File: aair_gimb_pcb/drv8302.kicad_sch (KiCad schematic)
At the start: 15 parts, among them U1 DRV8302

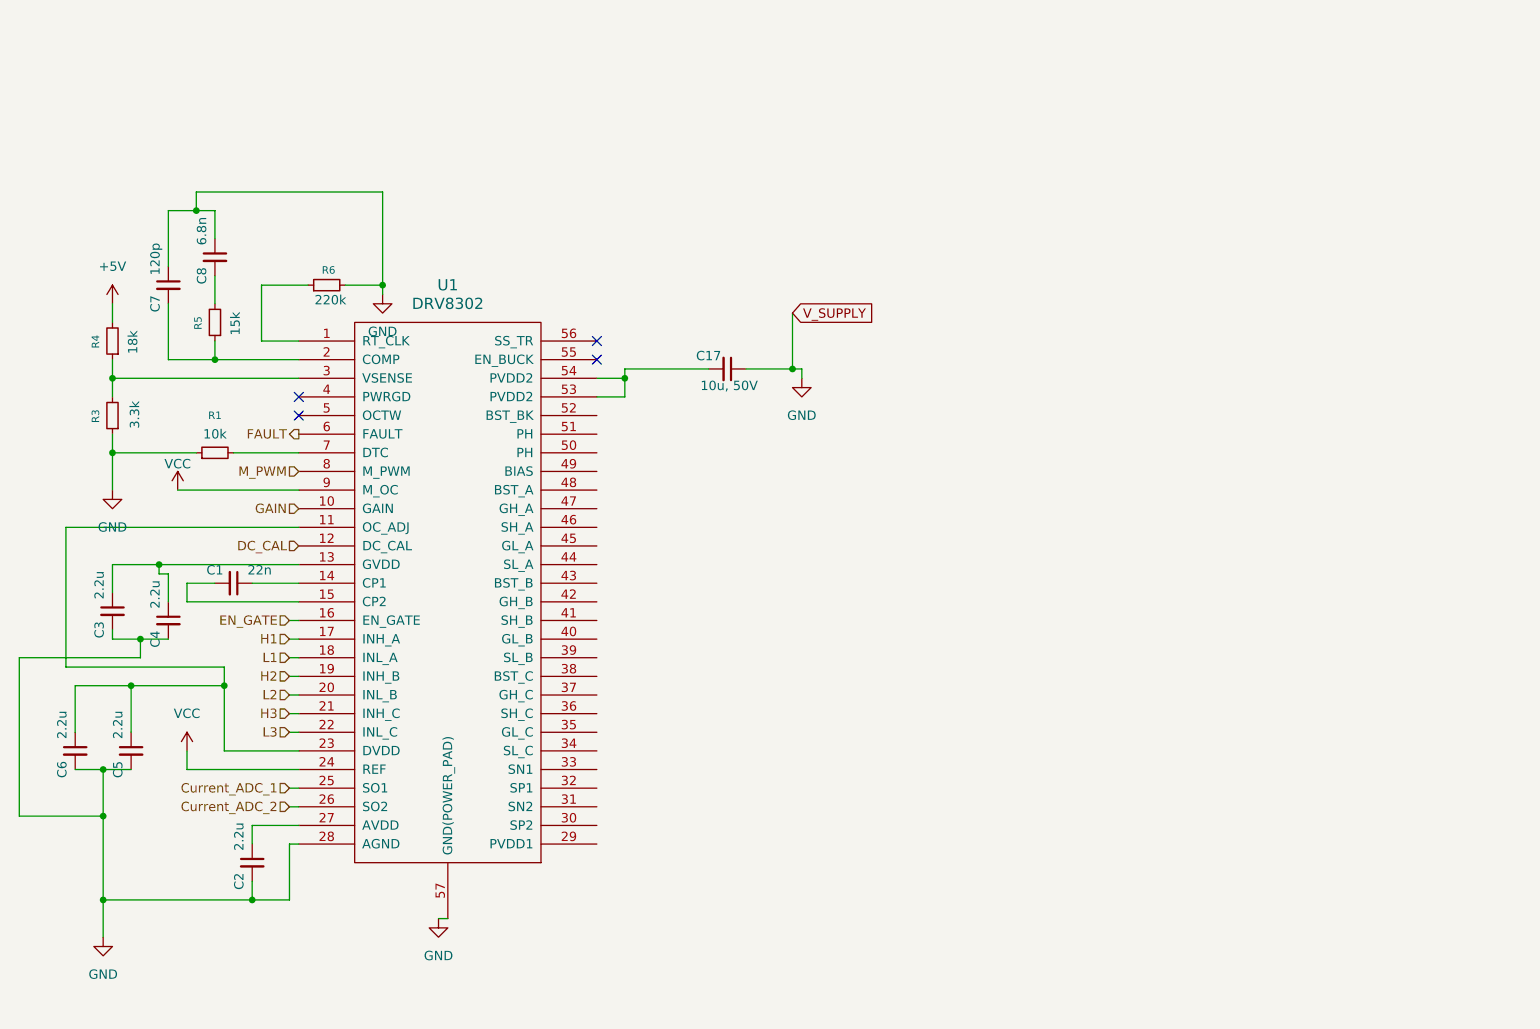
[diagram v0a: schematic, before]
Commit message: add mosfet
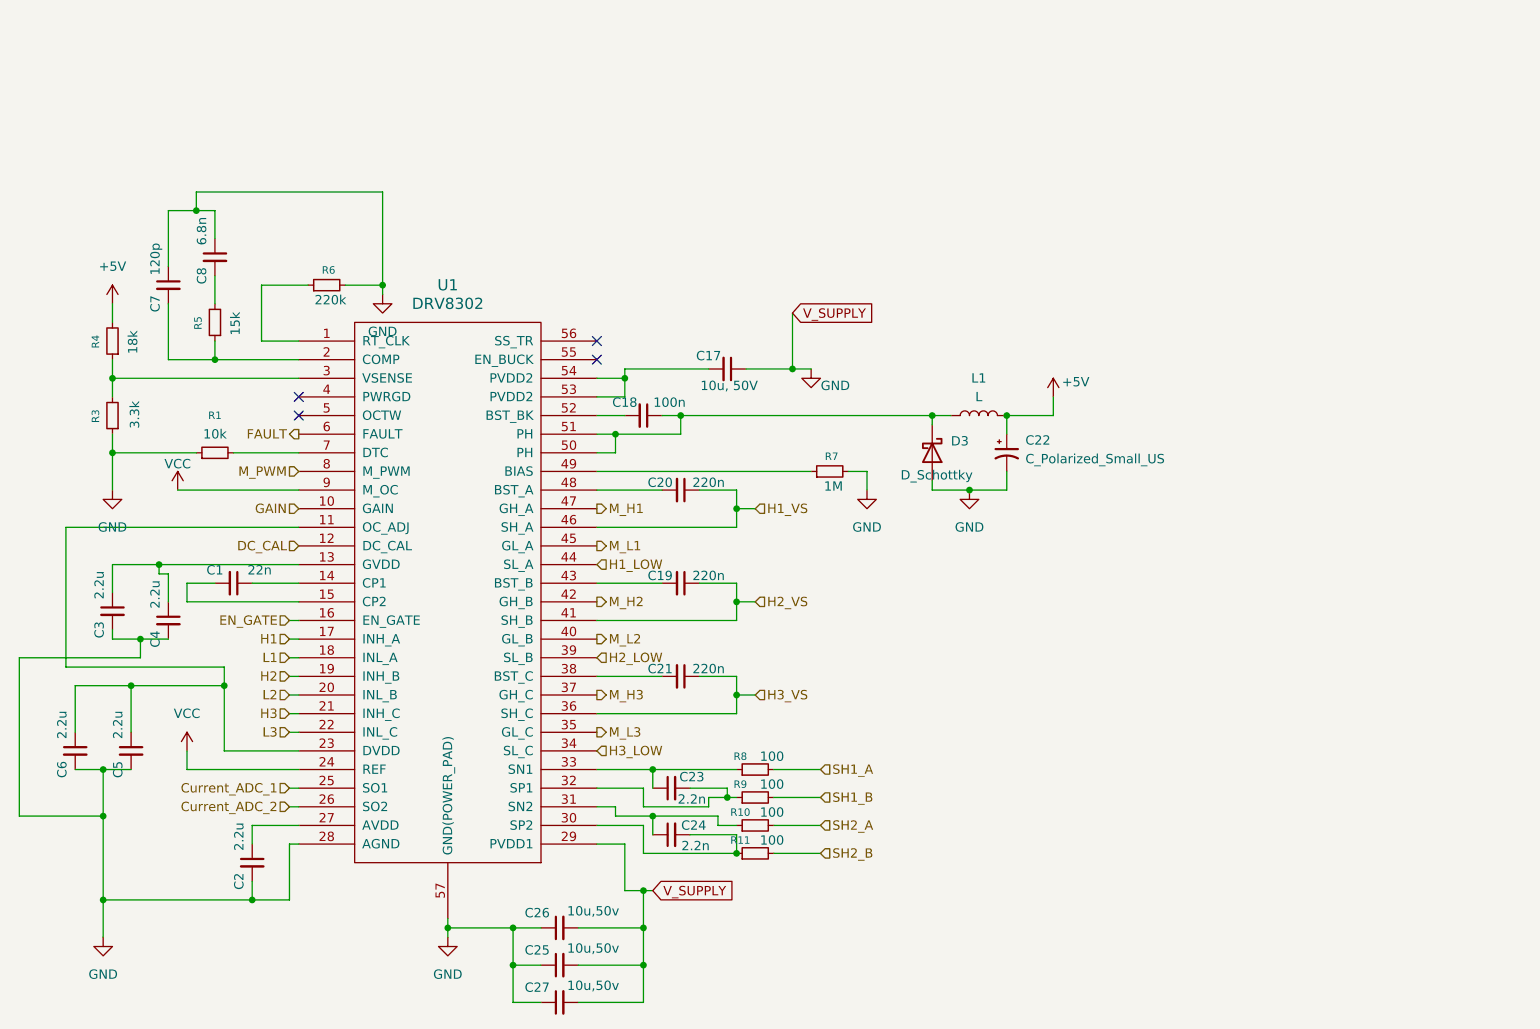
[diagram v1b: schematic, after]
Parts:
- added C18: 100n, CRF1:SMD-0603_r, symbol Device:C_Small
- added C19, C20, C21: 220n, CRF1:SMD-0603_r, symbol Device:C_Small
- added C22: C_Polarized_Small_US, Capacitor_Tantalum_SMD:CP_EIA-3528-21_Kemet-B, symbol Device:C_Polarized_Small_US
- added C23, C24: 2.2n, CRF1:SMD-0603_r, symbol Device:C_Small
- added C25, C26, C27: 10u,50v, Capacitor_SMD:C_1206_3216Metric, symbol Device:C_Small
- added D3: D_Schottky, Diode_SMD:D_SMA_Handsoldering, symbol Device:D_Schottky
- added L1: L, Inductor_SMD_Wurth:L_Wurth_WE-LQSH-2010, symbol Device:L
- added R10, R11, R8, R9: 100, CRF1:SMD-0603_r, symbol Device:R_Small
- added R7: 1M, CRF1:SMD-0603_r, symbol Device:R_Small
- R1, R3, R4, R5: footprint (none) -> CRF1:SMD-0603_r
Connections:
- net +5V: now also C22.1, L1.2
- net GND: now also U1.29 (PVDD1), C22.2, C25.1, C25.2, C26.1, C26.2, C27.1, C27.2, D3.2 (A), R7.2
- net at U1.30 (SP2): now also C24.2, R11.1
- net at U1.31 (SN2): now also C24.1, R10.1
- net at U1.32 (SP1): now also C23.2, R9.1
- net at U1.33 (SN1): now also C23.1, R8.1
- net H3_LOW: now reaches U1.34 (SL_C)
- net M_L3: now reaches U1.35 (GL_C)
- net H3_VS: now reaches U1.36 (SH_C)
- net H3_VS: now also C21.1
- net M_H3: now reaches U1.37 (GH_C)
- net at U1.38 (BST_C): now also C21.2
- net H2_LOW: now reaches U1.39 (SL_B)
- net M_L2: now reaches U1.40 (GL_B)
- net H2_VS: now reaches U1.41 (SH_B)
- net H2_VS: now also C19.1
- net M_H2: now reaches U1.42 (GH_B)
- net at U1.43 (BST_B): now also C19.2
- net H1_LOW: now reaches U1.44 (SL_A)
- net M_L1: now reaches U1.45 (GL_A)
- net H1_VS: now reaches U1.46 (SH_A)
- net H1_VS: now also C20.1
- net M_H1: now reaches U1.47 (GH_A)
- net at U1.48 (BST_A): now also C20.2
- net at U1.49 (BIAS): now also R7.1
- net at U1.50 (PH): now also U1.51 (PH), C18.1, D3.1 (K), L1.1
- net at U1.52 (BST_BK): now also C18.2
- new net SH1_A: R8.2
- new net SH1_B: R9.2
- new net SH2_A: R10.2
- new net SH2_B: R11.2

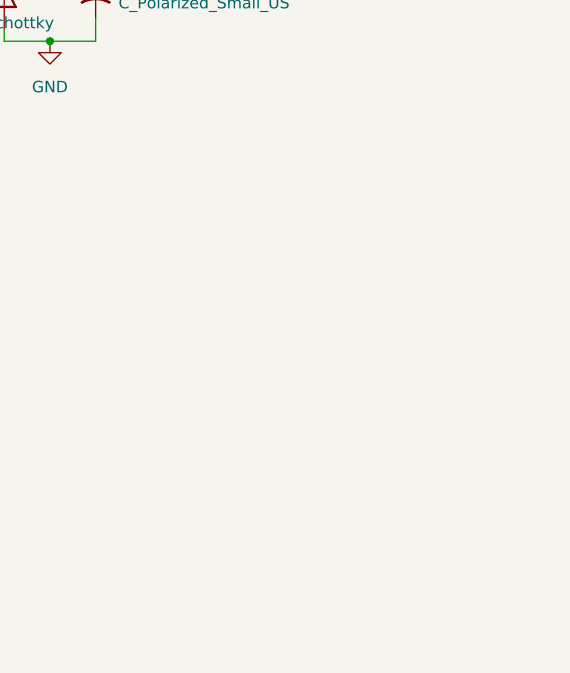
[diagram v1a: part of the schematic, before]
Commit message: добавить пины стм, диод, питание 3.3, разъемы
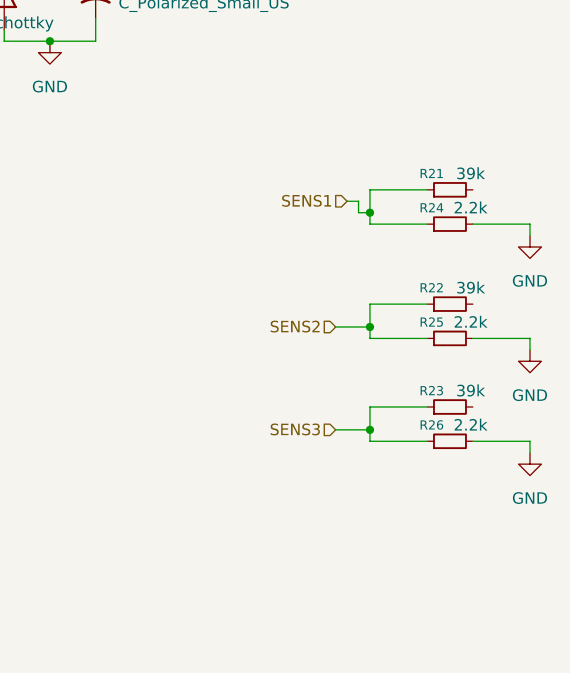
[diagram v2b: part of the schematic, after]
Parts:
- added R21, R22, R23: 39k, CRF1:SMD-0603_r, symbol Device:R_Small
- added R24, R25, R26: 2.2k, CRF1:SMD-0603_r, symbol Device:R_Small
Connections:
- net GND: now also R24.2, R25.2, R26.2
- new net SENS1: R21.1, R24.1
- new net SENS2: R22.1, R25.1
- new net SENS3: R23.1, R26.1

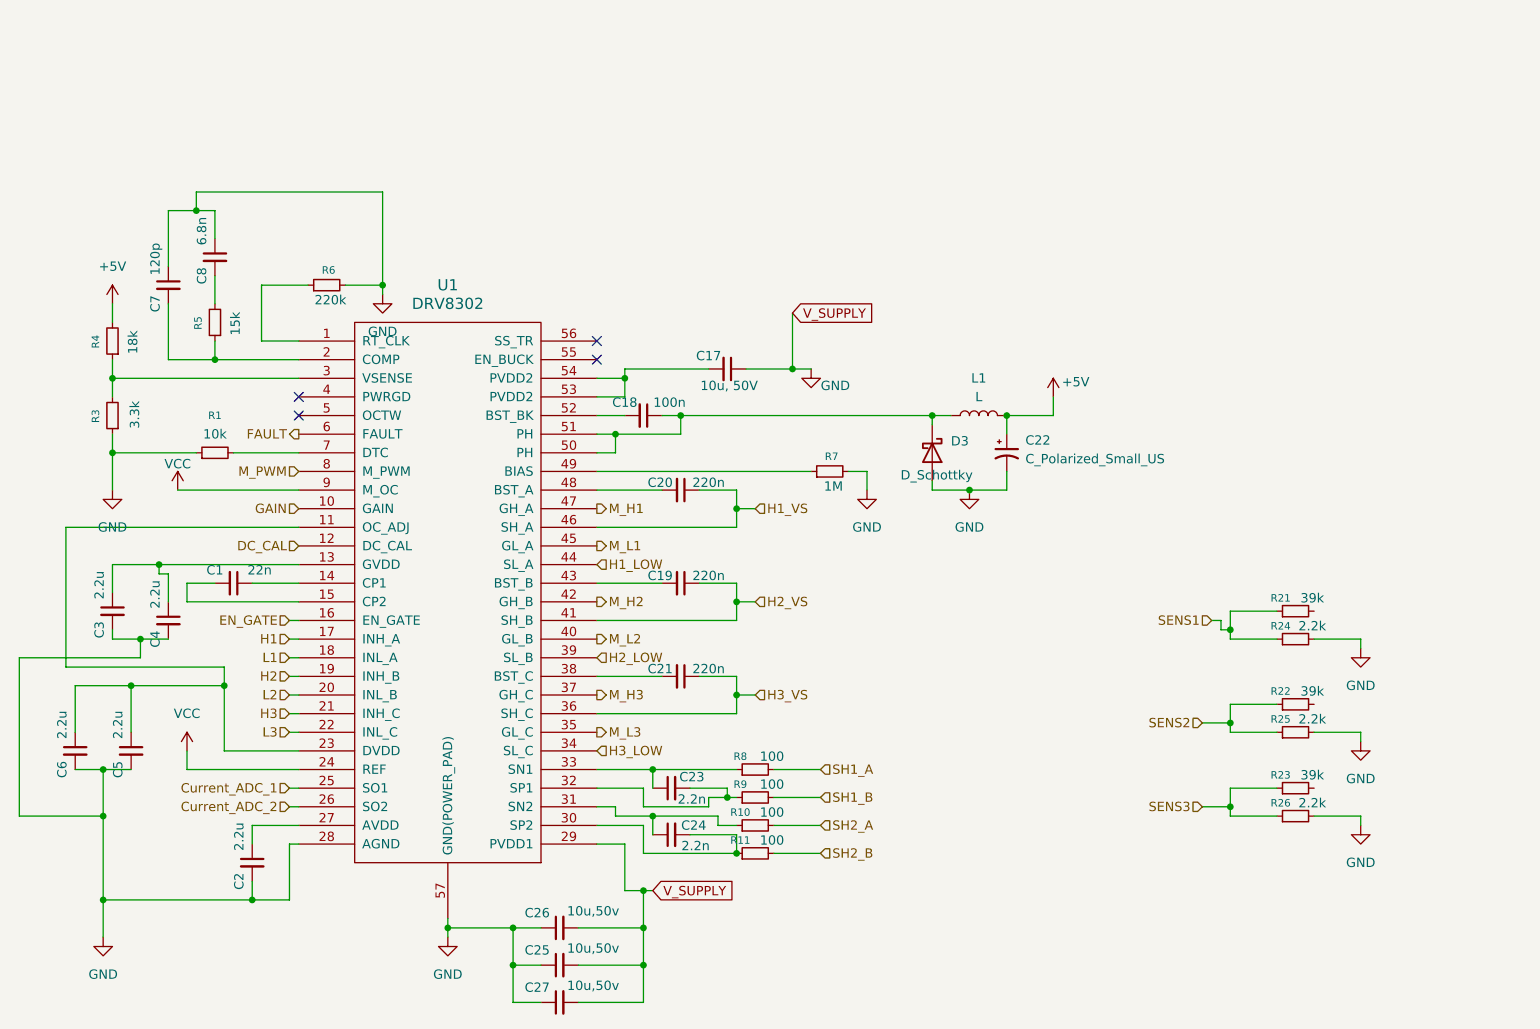
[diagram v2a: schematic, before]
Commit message: сделать коннектор для переыерии
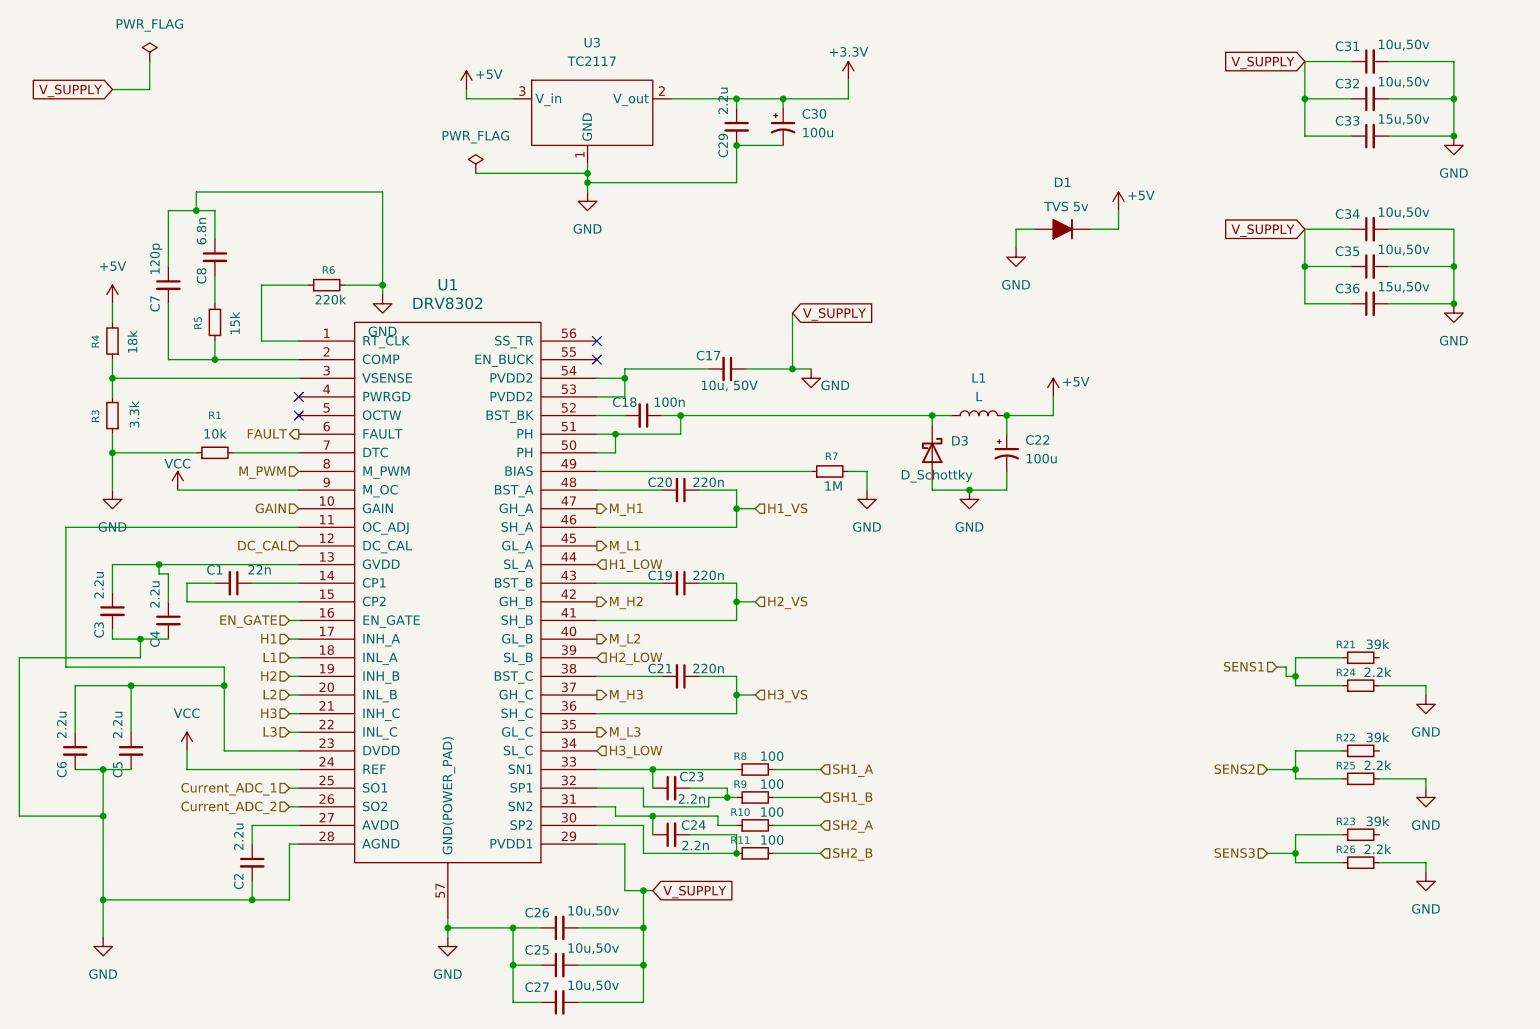
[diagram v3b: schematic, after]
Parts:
- added C29: 2.2u, CRF1:SMD-0603_r, symbol Device:C_Small
- added C30: 100u, Capacitor_Tantalum_SMD:CP_EIA-3528-21_Kemet-B, symbol Device:C_Polarized_Small_US
- added C31, C32, C34, C35: 10u,50v, Capacitor_SMD:C_1206_3216Metric, symbol Device:C_Small
- added C33, C36: 15u,50v, Capacitor_SMD:C_1206_3216Metric, symbol Device:C_Small
- added D1: TVS 5v, Diode_SMD:D_SMA, symbol Device:D_Filled
- added U3: TC2117, CRF1:SOT-223, symbol my_library:TC2117
- C22: value C_Polarized_Small_US -> 100u
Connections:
- net +5V: now also D1.1 (K), U3.3 (V_in)
- net GND: now also C29.2, C30.2, C31.1, C31.2, C32.1, C32.2, C33.1, C33.2, C34.1, C34.2, C35.1, C35.2, C36.1, C36.2, D1.2 (A), U3.1 (GND)
- new net +3.3V: C29.1, C30.1, U3.2 (V_out)
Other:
- moved on the sheet: R21, R22, R23, R24, R25, R26
